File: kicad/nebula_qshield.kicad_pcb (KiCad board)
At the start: 4 copper layers, 150 x 120 mm, 164 parts, among them J1 J1, J10 J10, J11 J11, J12 J12, J13 J13, J14 J14, J15 J15, J16 J16, J17 J17, J18 J18, J19 J19, J2 J2, J20 J20, J21 Arduino UNO Q Shield, J3 J3, J4 J4, J5 J5, J6 J6, J7 J7, J8 J8, J9 J9, K1 HF46F-12-HS1, K2 HF46F-12-HS1, Q1 IRLZ44NPBF, Q2 IRLZ44NPBF, Q3 2N7002, Q4 2N7002, Q5 IRLZ44NPBF, SW1 RESET, T1 Transformer_SP_2S, T2 Transformer_SP_2S, T3 Transformer_SP_2S, U1 TPS54302DDCR, U10 MCP6002, U11 MCP6002, U12 SN6501, U13 AMC1301, U14 HX711, U15 MAX485ESA, U16 PC817X2NIP, U17 IR2104SPBF, U18 PC817X1NIP, U19 PC817X1NIP, U2 AMS1117-3.3, U20 MCP6002, U21 ISO1541, U22 SC16IS740, U23 SN74LVC1G04, U3 TPS3823-33DBVR, U4 MCP6002, U5 SN6501, U6 AMC1301, U7 MCP6002, U8 SN6501, U9 AMC1301, Y1 1.8432MHz

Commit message: feat(pcb): Fase 6 — vías de potencia 0.5/0.2 y cierre de pares cortos, DRC 0, 65 unconnected
Co-Authored-By: Devin AI <158243242+devin-ai-integration[bot]@users.noreply.github.com>
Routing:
- net /3V3_RAIL: track 475.5 -> 489.4 mm, vias 33 -> 37
- net /5V_RAIL: vias 7 -> 14
- net /12V_RAIL: vias 2 -> 6
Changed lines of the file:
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@@
 	)
 	(via
+		(at 16.960725 102.548222)
+		(size 0.5)
+		(drill 0.2)
+		(layers "F.Cu" "B.Cu")
+		(net "/3V3_RAIL")
+	)
+	(via
+		(at 66.738031 22.859044)
+		(size 0.5)
+		(drill 0.2)
+		(layers "F.Cu" "B.Cu")
+		(net "/3V3_RAIL")
+	)
+	(via
 		(at 8.0981 12.6929)
 		(size 0.8)
@@
 	)
 	(via
+		(at 21.6125 104.024491)
+		(size 0.5)
+		(drill 0.2)
+		(layers "F.Cu" "B.Cu")
+		(net "/3V3_RAIL")
+	)
+	(via
 		(at 71.673 34.8479)
 		(size 0.8)
@@
 	)
 	(via
+		(at 17.314347 107.451706)
+		(size 0.5)
+		(drill 0.2)
+		(layers "F.Cu" "B.Cu")
+		(net "/3V3_RAIL")
+	)
+	(via
 		(at 38.7423 1.9814)
 		(size 0.8)
@@
 	)
 	(segment
+		(start 22.2853 109.773)
+		(end 16.9607 102.5482)
+		(width 0.5)
+		(layer "B.Cu")
+		(net "/3V3_RAIL")
+	)
+	(segment
 		(start 64.6323 22.5072)
 		(end 65.5976 22.5072)
@@
 	)
 	(segment
+		(start 16.960725 102.548222)
+		(end 17.314347 107.451706)
+		(width 0.5)
+		(layer "B.Cu")
+		(net "/3V3_RAIL")
+	)
+	(segment
 		(start 31.5435 96.8105)
 		(end 30.8445 96.1115)
@@
 	)
 	(via
+		(at 78.05 18.05)
+		(size 0.5)
+		(drill 0.2)
+		(layers "F.Cu" "B.Cu")
+		(net "/5V_RAIL")
+	)
+	(via
 		(at 3.4984 10.8936)
 		(size 0.8)
@@
 	)
 	(via
+		(at 52.12 11.0625)
+		(size 0.5)
+		(drill 0.2)
+		(layers "F.Cu" "B.Cu")
+		(net "/5V_RAIL")
+	)
+	(via
+		(at 19.9 12.879694)
+		(size 0.5)
+		(drill 0.2)
+		(layers "F.Cu" "B.Cu")
+		(net "/5V_RAIL")
+	)
+	(via
 		(at 55.8313 11.0893)
 		(size 0.8)
@@
 	)
 	(via
+		(at 56.2625 28.15)
+		(size 0.5)
+		(drill 0.2)
+		(layers "F.Cu" "B.Cu")
+		(net "/5V_RAIL")
+	)
+	(via
+		(at 21.32 7.87)
+		(size 0.5)
+		(drill 0.2)
+		(layers "F.Cu" "B.Cu")
+		(net "/5V_RAIL")
+	)
+	(via
+		(at 69.869915 16.980222)
+		(size 0.5)
+		(drill 0.2)
+		(layers "F.Cu" "B.Cu")
+		(net "/5V_RAIL")
+	)
+	(via
 		(at 52.2746 -0.581)
 		(size 0.8)
@@
 		(net "/5V_RAIL")
 	)
+	(via
+		(at 59.373258 14.984811)
+		(size 0.5)
+		(drill 0.2)
+		(layers "F.Cu" "B.Cu")
+		(net "/5V_RAIL")
+	)
 	(segment
 		(start 123.777 79.3778)
@@
 	)
 	(via
+		(at 10.175 24)
+		(size 0.5)
+		(drill 0.2)
+		(layers "F.Cu" "B.Cu")
+		(net "/12V_RAIL")
+	)
+	(via
 		(at 112.1214 73.8959)
 		(size 0.5)
@@
 	)
 	(via
+		(at 14.15 20.05)
+		(size 0.5)
+		(drill 0.2)
+		(layers "F.Cu" "B.Cu")
+		(net "/12V_RAIL")
+	)
+	(via
+		(at 14.748258 23.633111)
+		(size 0.5)
+		(drill 0.2)
+		(layers "F.Cu" "B.Cu")
+		(net "/12V_RAIL")
+	)
+	(via
 		(at 112.1214 76.4359)
 		(size 0.5)
 		(drill 0.2)
+		(layers "F.Cu" "B.Cu")
+		(net "/12V_RAIL")
+	)
+	(via
+		(at 14.925 23.8)
+		(size 0.5)
+		(drill 0.2)

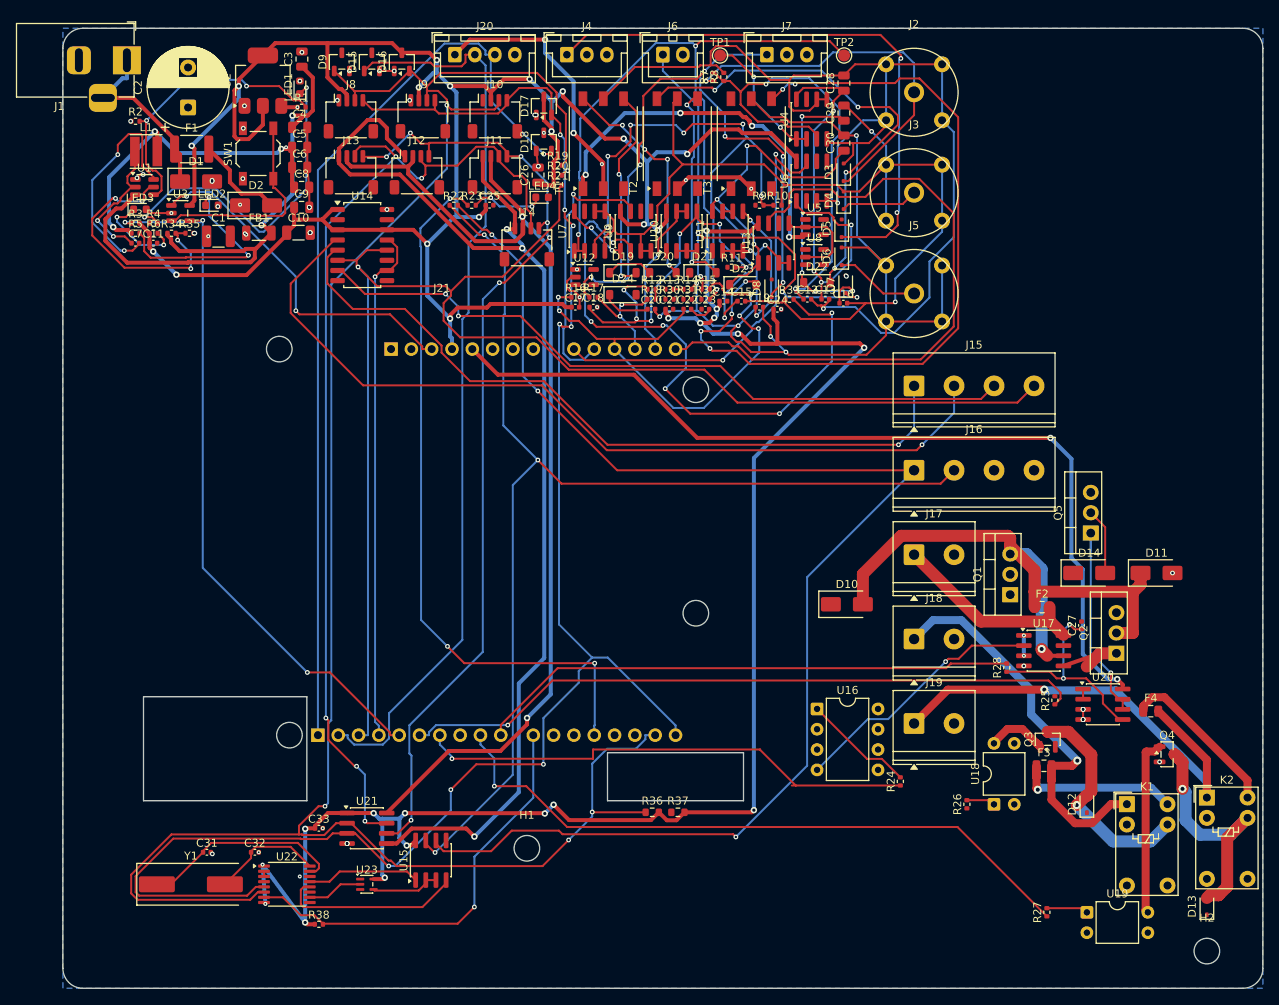
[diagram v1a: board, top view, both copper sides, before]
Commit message: feat(pcb): Fase 6 — vías de potencia 0.5/0.2 y cierre de pares cortos, DRC 0, 62 unconnected
Co-Authored-By: Devin AI <158243242+devin-ai-integration[bot]@users.noreply.github.com>
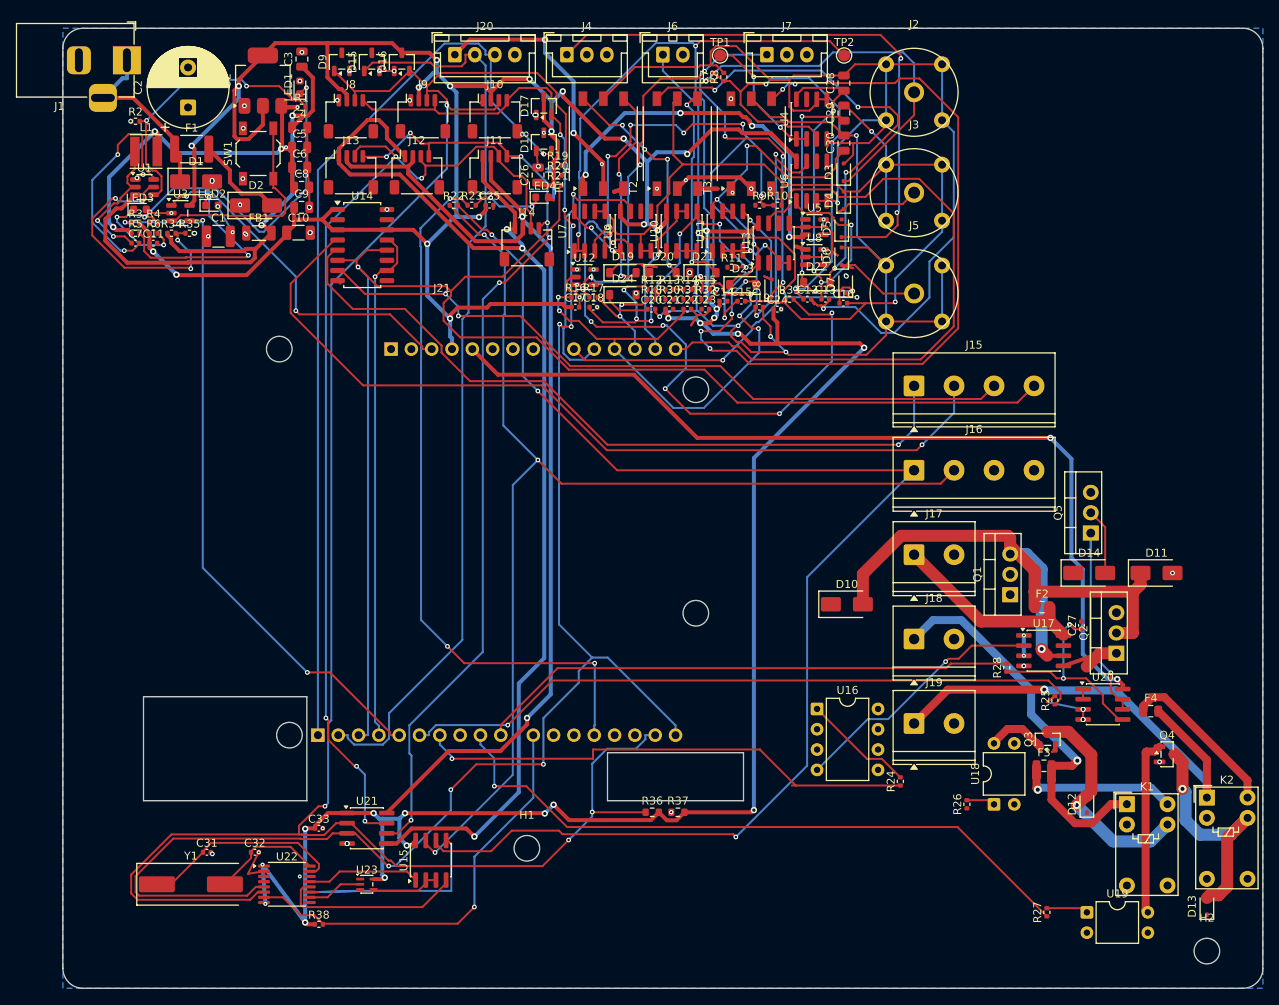
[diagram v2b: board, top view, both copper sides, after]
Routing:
- net GND: track 44.5 -> 125.8 mm, vias 50 -> 51
- net /5V_RAIL: track 202.4 -> 211.0 mm, vias 14 -> 15
- net /Analog Acquisition/SN_D2_ORP: track 0.00 -> 5.00 mm, vias 0 -> 2
- net /Analog Acquisition/VDD_ISO_PH: track 58.8 -> 62.8 mm
- net /Analog Acquisition/DO_SIG: track 10.5 -> 13.5 mm
- net /Analog Acquisition/SN_D2_PH: track 0.00 -> 2.50 mm, vias 0 -> 1
- net /3V3_RAIL: track 489.4 -> 491.4 mm
- net /Analog Acquisition/VDD_ISO_ORP: track 44.7 -> 46.2 mm, vias 6 -> 8
- net /Analog Acquisition/GND_ISO_PH: track 147.5 -> 149.0 mm
- net /Analog Acquisition/ORP_SIG: track 9.65 -> 11.1 mm
- net /12V_RAIL: track 2.68 -> 3.68 mm, vias 6 -> 9
- net /Analog Acquisition/VDD_ISO_DO: track 46.7 -> 47.7 mm
- net /Analog Acquisition/PH_BUF: track 16.9 -> 17.4 mm
- net /I2C_SCL: vias 9 -> 11
- net /Analog Acquisition/SN_D2_DO: vias 0 -> 2
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
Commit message: feat(pcb): Fase 6b — close_pairs_v5 con proyección a tracks, DRC 0, 49 unconnected
Co-Authored-By: Devin AI <158243242+devin-ai-integration[bot]@users.noreply.github.com>
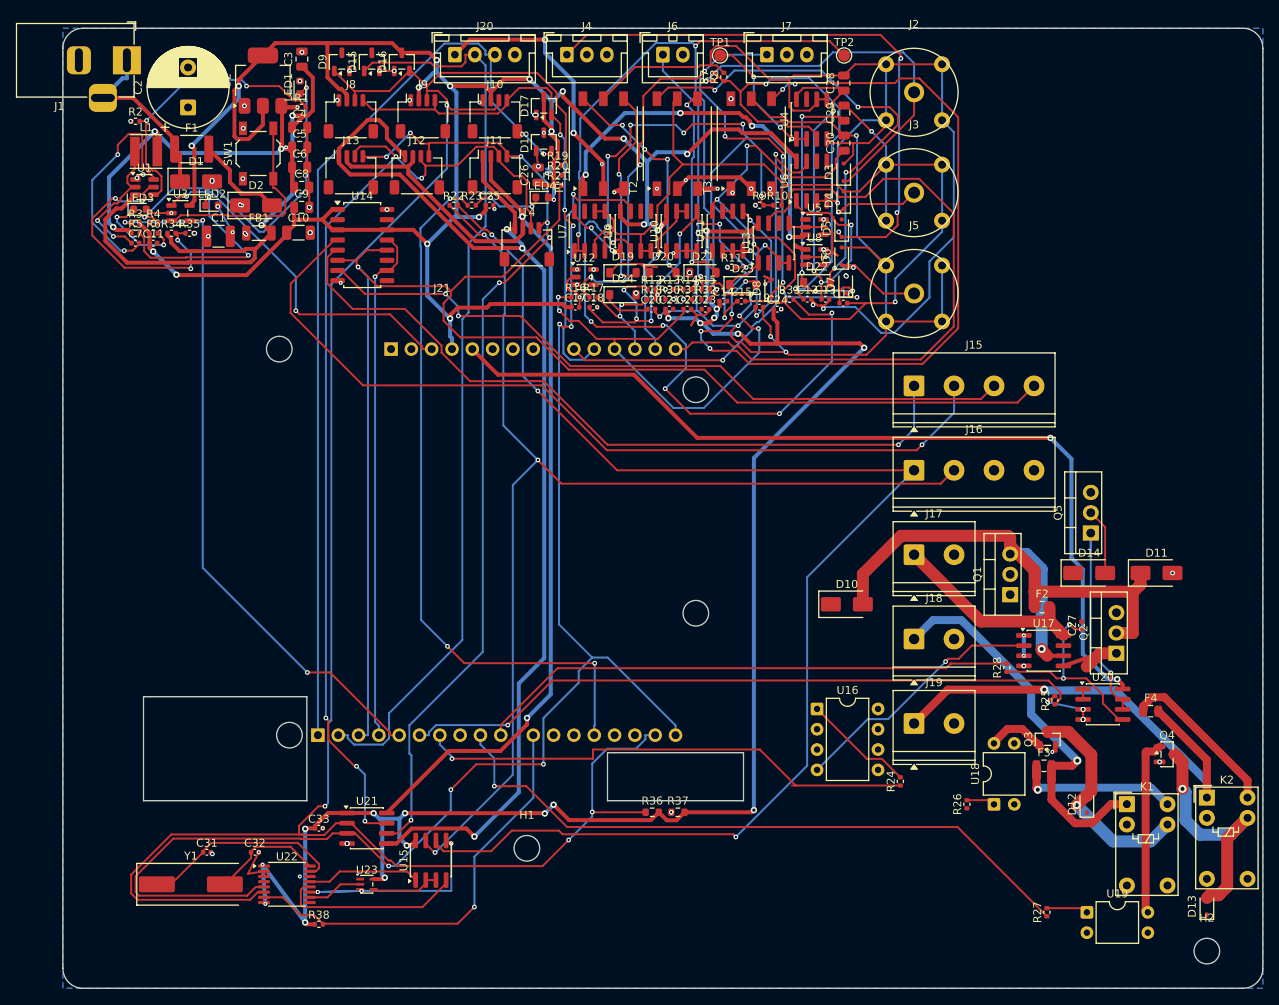
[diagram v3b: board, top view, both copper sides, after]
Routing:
- net GND: track 125.8 -> 137.9 mm, vias 51 -> 75
- net /Analog Acquisition/DO_SIG: track 13.5 -> 15.0 mm, vias 0 -> 2
- net /Analog Acquisition/SN_D2_PH: track 2.50 -> 3.75 mm, vias 1 -> 3
- net /Analog Acquisition/VDD_ISO_ORP: track 46.2 -> 46.9 mm, vias 8 -> 12
- net /3V3_RAIL: track 491.4 -> 492.1 mm, vias 37 -> 39
- net /Analog Acquisition/CO2_SIG: track 72.9 -> 73.7 mm, vias 2 -> 4
- net /Analog Acquisition/GND_ISO_PH: track 149.0 -> 149.7 mm, vias 2 -> 4
- net /12V_RAIL: track 3.68 -> 4.18 mm, vias 9 -> 13
- net /I2C_SCL: vias 11 -> 13
- net /Analog Acquisition/SN_D2_ORP: vias 2 -> 4
- net /Analog Acquisition/SN_D2_DO: vias 2 -> 4
- net /Analog Acquisition/SN_D1_DO: vias 2 -> 4
- net /Analog Acquisition/PH_BUF: vias 2 -> 4
- net /Analog Acquisition/ORP_SIG: vias 0 -> 2
- net /Analog Acquisition/DO_SEC_B: vias 2 -> 4

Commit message: feat(pcb): Fase 6c — close_pairs_v5 con ajuste a puntos exactos de endpoints, DRC 0, 45 unconnected
Co-Authored-By: Devin AI <158243242+devin-ai-integration[bot]@users.noreply.github.com>
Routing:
- net /3V3_RAIL: track 492.1 -> 498.0 mm, vias 39 -> 41
- net /Analog Acquisition/PH_ATT: track 0.00 -> 5.17 mm
- net unconnected-(K2-Pad5): track 0.00 -> 5.08 mm
- net unconnected-(K1-Pad5): track 0.00 -> 5.08 mm
- net /HUM_ADC: track 13.7 -> 17.1 mm
- net GND: track 137.9 -> 140.9 mm, vias 75 -> 81
- net /Analog Acquisition/VDD_ISO_DO: track 47.7 -> 50.7 mm, vias 3 -> 5
- net /Analog Acquisition/SN_D2_ORP: track 5.00 -> 7.50 mm, vias 4 -> 6
- net /Analog Acquisition/ORP_SIG: track 11.1 -> 13.6 mm, vias 2 -> 4
- net /Analog Acquisition/DO_SIG: track 15.0 -> 16.5 mm, vias 2 -> 4
- net /Analog Acquisition/SN_D2_PH: track 3.75 -> 5.00 mm, vias 3 -> 5
- net /12V_RAIL: track 4.18 -> 4.93 mm, vias 13 -> 17
- net /Analog Acquisition/VDD_ISO_ORP: track 46.9 -> 47.7 mm, vias 12 -> 16
- net /Actuator Drivers/MOTOR_HO: track 0.00 -> 0.75 mm, vias 0 -> 2
- net /Analog Acquisition/CO2_SIG: track 73.7 -> 74.4 mm, vias 4 -> 6
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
